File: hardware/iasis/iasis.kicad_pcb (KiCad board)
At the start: 6 copper layers, 125 x 89 mm, 658 parts, among them J1001 USB4105-GF-A-120, J1101 SWD debug, J1131 SM04B-SRSS-TB, J1132 UART debug, J401 1054500101, J501 1054500101, J601 1054500101, J701 1054500101, J801 1054500101, J901 1054500101, Q1001 CSD18543Q3A, Q1002 CSD18543Q3A, Q1221 2N7002, Q1230 2N7002, Q1231 2N7002, Q1232 2N7002, Q1321 2N7002, Q1330 2N7002, Q1331 2N7002, Q1332 2N7002, Q1421 2N7002, Q1430 2N7002, Q1431 2N7002, Q1432 2N7002, Q1521 2N7002, Q1530 2N7002, Q1531 2N7002, Q1532 2N7002, Q1621 2N7002, Q1630 2N7002, Q1631 2N7002, Q1632 2N7002, Q1911 2N7002, Q1912 2N7002, SW1101 PTS645SL50SMTR92LFS, SW1102 PTS645SL50SMTR92LFS, SW1171 PTS645SL50SMTR92LFS, U1001 LM74502DDFR, U1002 CH224Q, U1003 TPS26600PWPR, U1040 AP3441SHE-7B, U1060 AP3441SHE-7B, U1080 TPS3808G33DBVR, U1101 RP2354B, U1131 TCA9548APWR, U1141 TMUX1511PWR, U1142 TMUX1511PWR, U1171 SN74AHCT1G125DBVR, U1172 TCA6408ARGTR, U1181 74HC595D,118, U1182 74HC595D,118, U1202 TPS259470LRPWR, U1203 74LVC2G08DC-Q100H, U1230 LMR51450SDRRR, U1231 TPS26600PWPR, U1232 LM4040DIM3X-2.5/NOPB, U1302 TPS259470LRPWR, U1303 74LVC2G08DC-Q100H, U1330 LMR51450SDRRR, U1331 TPS26600PWPR, U1332 LM4040DIM3X-2.5/NOPB, U1402 TPS259470LRPWR, U1403 74LVC2G08DC-Q100H, U1430 LMR51450SDRRR, U1431 TPS26600PWPR, U1432 LM4040DIM3X-2.5/NOPB, U1502 TPS259470LRPWR, U1503 74LVC2G08DC-Q100H, U1530 LMR51450SDRRR, U1531 TPS26600PWPR, U1532 LM4040DIM3X-2.5/NOPB, U1602 TPS259470LRPWR, U1603 74LVC2G08DC-Q100H, U1630 LMR51450SDRRR, U1631 TPS26600PWPR, U1632 LM4040DIM3X-2.5/NOPB, U1901 AP22653W6-7, U1902 TPS259470LRPWR, U201 USB7206CT/KDX, U204 SN74AUP1G08DCKR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

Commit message: Reassign RP2354 GPIOs by package side and reorder the LED chain
With the controller turned 90 degrees, charge-cell requests and faults
leave the top, upper-right and left of the package towards the charging
row, and the data-cell lines (orientation, PD interrupt, CC fault) leave
the bottom in port order. ADC channels stay on GPIO40-47, UART on
GPIO0/1, I2C on GPIO24/25.

The SK6812 chain now runs from the host LED at the front right through
ports 5 to 1, matching the board. Update PCB also adds the Hub-variant
DNP flags the swapped charging inductors and capacitors were missing.
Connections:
- D1171 pad 1: /Indicators and confirmation/LED_DIN1 -> /Indicators and confirmation/LED_DIN5
- D1171 pad 3: /Indicators and confirmation/LED_DIN2 -> unconnected-(D1171-DOUT-Pad3)
- D1172 pad 1: /Indicators and confirmation/LED_DIN2 -> /Indicators and confirmation/LED_DIN4
- D1172 pad 3: /Indicators and confirmation/LED_DIN3 -> /Indicators and confirmation/LED_DIN5
- D1174 pad 1: /Indicators and confirmation/LED_DIN4 -> /Indicators and confirmation/LED_DIN2
- D1174 pad 3: /Indicators and confirmation/LED_DIN5 -> /Indicators and confirmation/LED_DIN3
- D1175 pad 1: /Indicators and confirmation/LED_DIN5 -> /Indicators and confirmation/LED_DIN1
- D1175 pad 3: unconnected-(D1175-DOUT-Pad3) -> /Indicators and confirmation/LED_DIN2
- U1101 pad 1: P4_HOST_EN_REQ -> HOST_BUDGET_FAULT_N
- U1101 pad 11: P2_HOST_EN_REQ -> P3_ORIENTATION
- U1101 pad 12: P1_CHARGE_EN_REQ -> P3_PD_IRQ_N
- U1101 pad 13: CONFIRM_N -> P4_CC_FAULT_MCU
- U1101 pad 14: P1_HOST_EN_REQ -> P4_ORIENTATION
- U1101 pad 16: HOST_BUDGET_FAULT_N -> P4_PD_IRQ_N
- U1101 pad 17: LED_DATA -> P5_CC_FAULT_MCU
- U1101 pad 18: P1_ORIENTATION -> P5_ORIENTATION
- U1101 pad 19: P2_ORIENTATION -> P5_PD_IRQ_N
- U1101 pad 2: P4_CHARGE_EN_REQ -> P1_CC_FAULT_MCU
- U1101 pad 20: P1_PD_IRQ_N -> LED_DATA
- U1101 pad 21: P2_PD_IRQ_N -> CONFIRM_N
- U1101 pad 22: P3_ORIENTATION -> TCA_RESET_N
- U1101 pad 23: P1_CC_FAULT_MCU -> P5_POWER_FAULT_N
- U1101 pad 25: P2_CC_FAULT_MCU -> MCU_I2C_SDA
- U1101 pad 26: P3_PD_IRQ_N -> MCU_I2C_SCL
- U1101 pad 27: P3_CC_FAULT_MCU -> P5_CHARGE_EN_REQ
- U1101 pad 28: P4_CC_FAULT_MCU -> P5_HOST_EN_REQ
- U1101 pad 3: P1_POWER_FAULT_N -> P1_ORIENTATION
- U1101 pad 36: P5_CC_FAULT_MCU -> P4_POWER_FAULT_N
- U1101 pad 37: P4_ORIENTATION -> P4_CHARGE_EN_REQ
- U1101 pad 38: P4_PD_IRQ_N -> SHIFT_OE_N
- U1101 pad 39: P5_ORIENTATION -> P4_HOST_EN_REQ
- U1101 pad 4: P3_POWER_FAULT_N -> P2_CC_FAULT_MCU
- U1101 pad 40: P5_PD_IRQ_N -> EXP_RESET_N
- U1101 pad 42: EXP_RESET_N -> P3_POWER_FAULT_N
- U1101 pad 43: MCU_I2C_SDA -> P3_CHARGE_EN_REQ
- U1101 pad 44: MCU_I2C_SCL -> P3_HOST_EN_REQ
- U1101 pad 45: TCA_RESET_N -> P2_POWER_FAULT_N
- U1101 pad 46: SHIFT_OE_N -> P2_HOST_EN_REQ
- U1101 pad 47: P5_POWER_FAULT_N -> P2_CHARGE_EN_REQ
- U1101 pad 48: P5_CHARGE_EN_REQ -> P1_HOST_EN_REQ
- U1101 pad 49: VSYS_SENSE -> P1_VBUS_ADC
- U1101 pad 52: P5_VBUS_ADC -> P2_VBUS_ADC
- U1101 pad 53: P4_VBUS_ADC -> P3_VBUS_ADC
- U1101 pad 54: P2_VBUS_ADC -> P4_VBUS_ADC
- U1101 pad 55: P3_VBUS_ADC -> VSYS_SENSE
- U1101 pad 56: P1_VBUS_ADC -> P5_VBUS_ADC
- U1101 pad 57: TEMP_BANK_A -> TEMP_BANK_B
- U1101 pad 58: TEMP_BANK_B -> TEMP_BANK_A
- U1101 pad 6: P3_HOST_EN_REQ -> P1_PD_IRQ_N
- U1101 pad 7: P2_CHARGE_EN_REQ -> P2_ORIENTATION
- U1101 pad 79: P5_HOST_EN_REQ -> P1_POWER_FAULT_N
- U1101 pad 8: P3_CHARGE_EN_REQ -> P2_PD_IRQ_N
- U1101 pad 80: P4_POWER_FAULT_N -> P1_CHARGE_EN_REQ
- U1101 pad 9: P2_POWER_FAULT_N -> P3_CC_FAULT_MCU

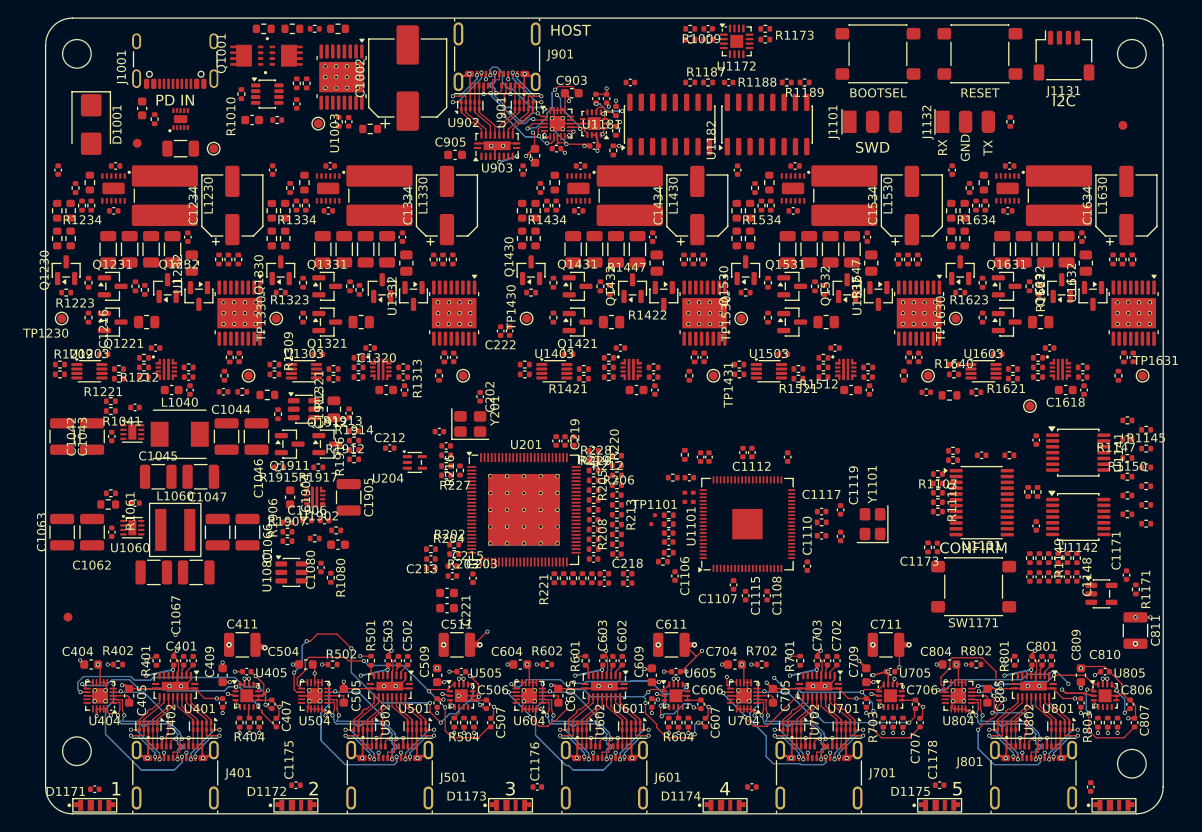
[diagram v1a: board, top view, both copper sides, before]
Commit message: Route the USB lanes
Every SuperSpeed, USB 2 and MCU USB pair now runs from the hub to its port,
the host connector or the controller, length-matched within each pair and
with ground return vias at the layer changes. Hub pins 94/95 take EXT_RX_N/P
so the upstream receive pair needs no crossing; the hub's receiver corrects
lane polarity.
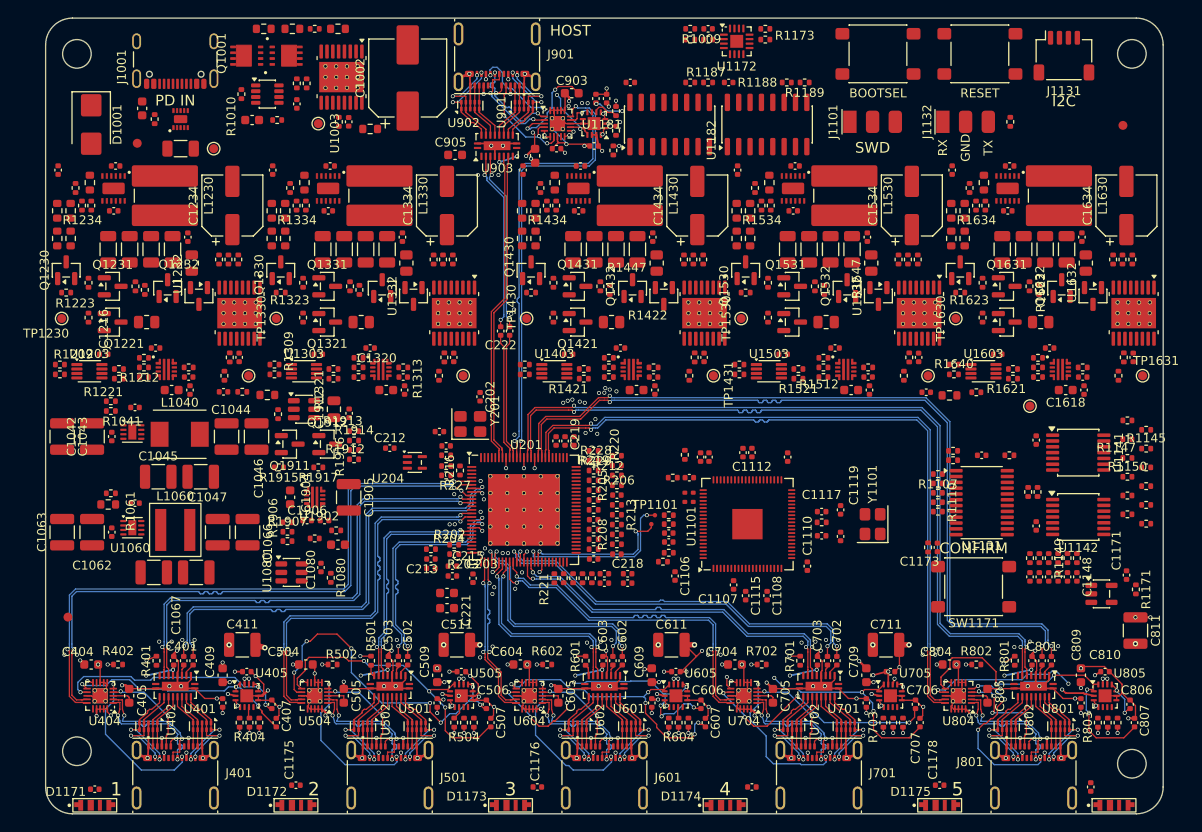
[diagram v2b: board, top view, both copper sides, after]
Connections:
- U201 pad 94: EXT_RX_P -> EXT_RX_N
- U201 pad 95: EXT_RX_N -> EXT_RX_P
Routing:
- net P5_TX_RAW_P: track 0.00 -> 89.0 mm, vias 0 -> 2
- net P5_TX_RAW_N: track 0.00 -> 89.0 mm, vias 0 -> 2
- net P5_RX_P: track 0.00 -> 88.9 mm, vias 0 -> 2
- net P5_RX_N: track 0.00 -> 88.9 mm, vias 0 -> 2
- net P5_USB2_D_N: track 0.00 -> 79.1 mm, vias 0 -> 2
- net P5_USB2_D_P: track 0.00 -> 79.1 mm, vias 0 -> 2
- net P1_USB2_D_N: track 0.00 -> 70.3 mm, vias 0 -> 2
- net P1_USB2_D_P: track 0.00 -> 70.3 mm, vias 0 -> 2
- net P1_RX_P: track 0.00 -> 53.4 mm, vias 0 -> 2
- net P1_RX_N: track 0.00 -> 53.4 mm, vias 0 -> 2
- net P1_TX_RAW_P: track 0.00 -> 51.4 mm, vias 0 -> 2
- net P1_TX_RAW_N: track 0.00 -> 51.4 mm, vias 0 -> 2
- net EXT_D_P: track 0.00 -> 49.9 mm, vias 0 -> 2
- net EXT_D_N: track 0.00 -> 49.9 mm, vias 0 -> 2
- net P4_TX_RAW_N: track 0.00 -> 43.7 mm, vias 0 -> 2
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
